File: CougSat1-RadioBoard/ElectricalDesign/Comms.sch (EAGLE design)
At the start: 409 parts, among them J1 230mm Antenna, J2 CougSat Card, J3 700mm Antenna, J4 SWD, Q1 CSD25402Q3A, Q12 DMN53D0LDW, Q2 CSD25402Q3A, Q3 DMN53D0LDW, Q9 DMN53D0LDW, U1 INA199C1, U10 HMC452QS16G, U11 AD8515, U12 AD7291, U13 AD8515, U14 LP5907MFX-3.1, U15 AD9761, U16 TXS0102DQM, U18 TXS0102DQM, U19 MMZ09332B, U2 LP5907MFX-3.1, U20 ADF4360, U21 HMC545A, U22 AD9761, U23 MAAM-011229, U24 AD8515, U25 MAAM-011229, U26 AD8345, U28 AD8348, U29 AD7291, U3 TPS61236, U30 TXS0102DQM, U31 MAAM-011229, U32 AD8515, U35 TXS0102DQM, U36 ADF4360, U37 MAAM-011229, U39 AD8515, U4 AD8346, U40 AD8515, U42 TXS0102DQM, U43 INA199C2, U44 TXS0102DQM, U45 TXS0102DQM, U46 TXS0102DQM, U47 TXS0102DQM, U48 AD7291, U49 AD8515, U5 ADF4360, U50 INA199C2, U51 LP5907MFX-3.1, U52 INA199C2, U53 INA199C1, U54 TXS0102DQM, U55 TXS0102DQM, U6 STM32L496VGT, U7 GRF2133, U8 IS25LP016D, U9 IS25LP016D, Y1 19.68MHz ±2.5ppm, Y2 8MHz ±10ppm, Y3 32.768kHz ±10ppm, Y4 19.68MHz ±2.5ppm, Y5 19.68MHz ±2.5ppm

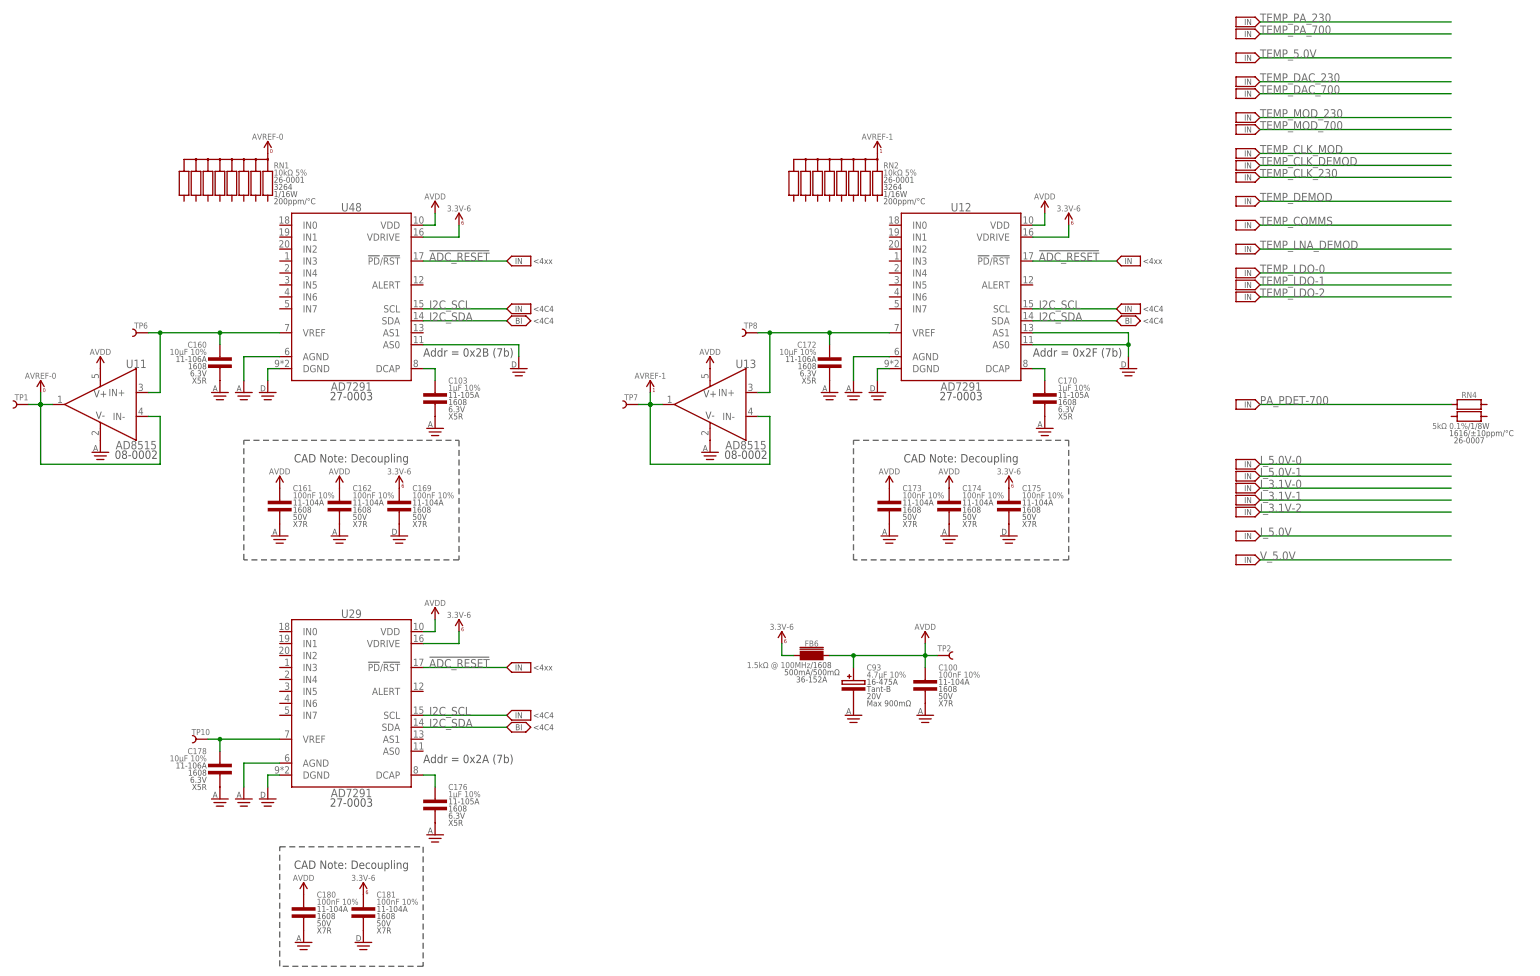
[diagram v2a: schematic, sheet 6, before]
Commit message: Laid out SPI bus, regulator, and JTAG
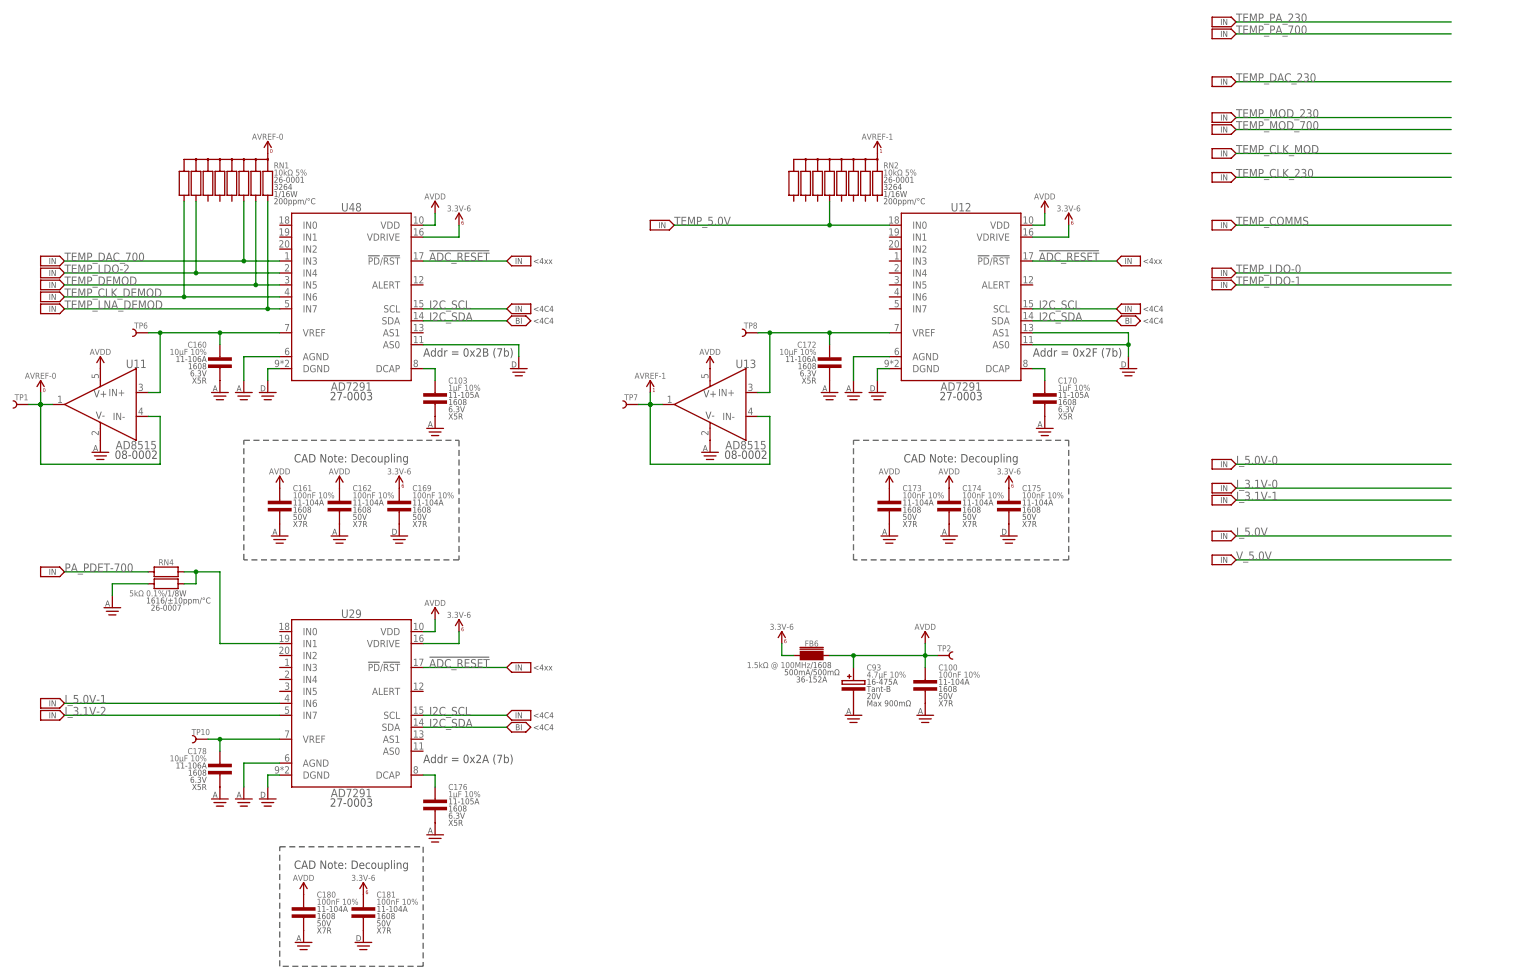
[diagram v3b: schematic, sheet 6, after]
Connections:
- net I_5.0V-1P renamed I_5.0V_1P
- new net ADC_PA_PDET-700: RN4.A2, RN4.B2, U29.IN1
- net AGND: now also RN4.A1
- net CTRL_SYNC: now also U6C.PC4; no longer U6C.PC6
- net I_3.1V-2: now also U29.IN7
- net I_5.0V-1: now also U29.IN6
- net TEMP_5.0V: now also RN2.5, U12.IN0
- net TEMP_CLK_DEMOD: now also RN1.8, U48.IN6
- net TEMP_DAC_700: now also RN1.3, U48.IN3
- net TEMP_DEMOD: now also RN1.2, U48.IN5
- net TEMP_LDO-2: now also RN1.7, U48.IN4
- net TEMP_LNA_DEMOD: now also RN1.1, U48.IN7
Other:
- moved on the sheet: RN4

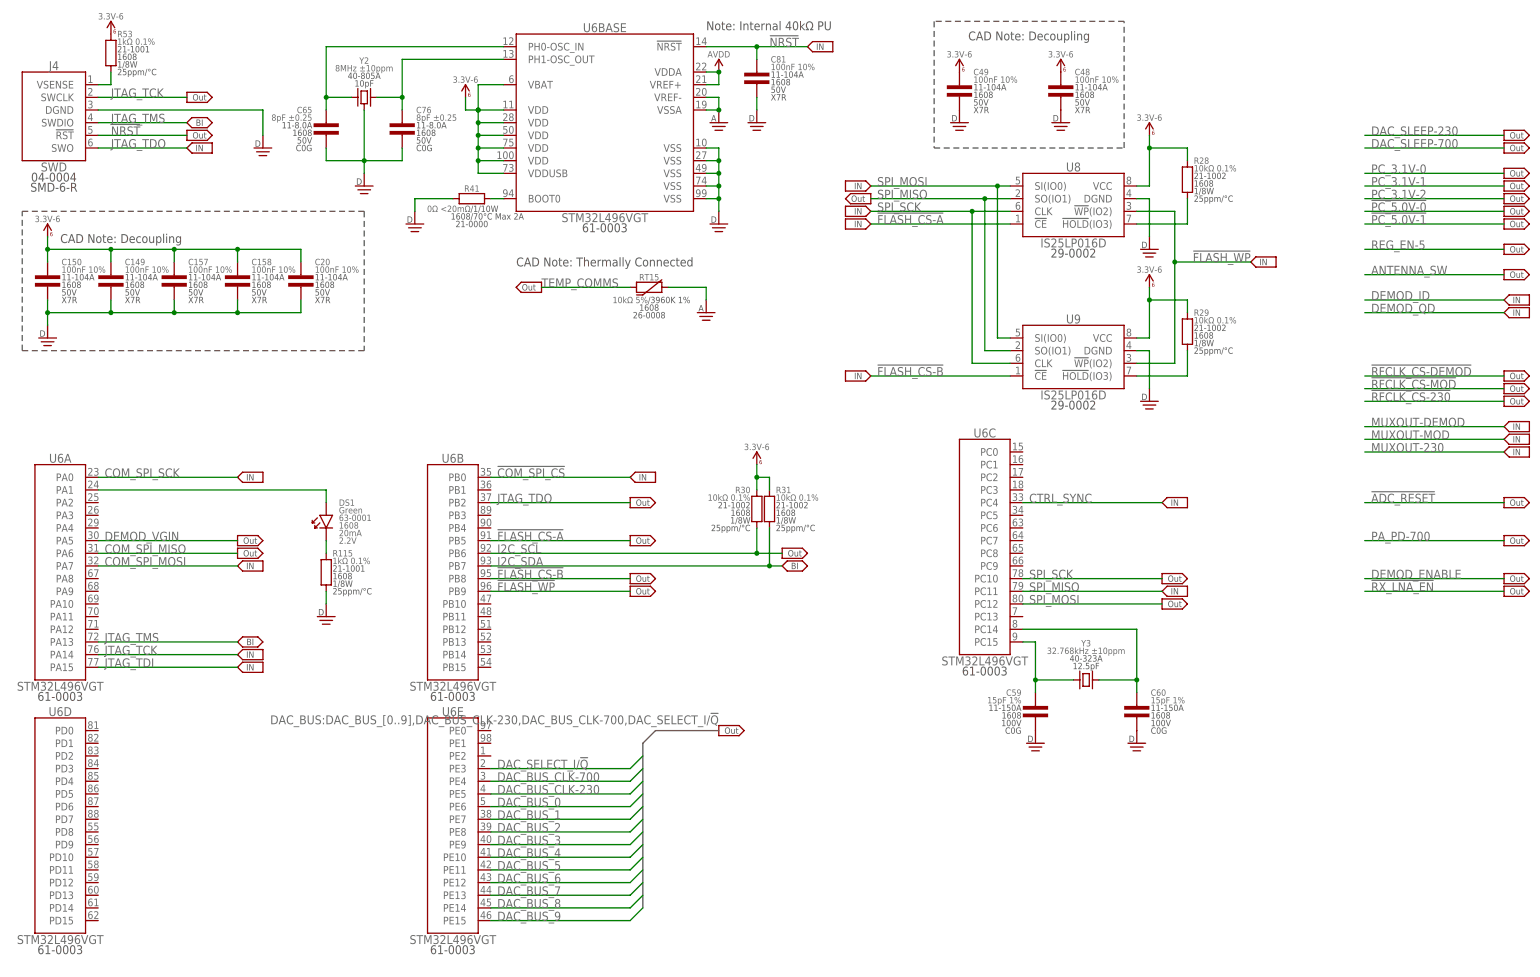
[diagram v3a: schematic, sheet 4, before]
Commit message: Laid out ADCs and 700mm thermistors and SPI
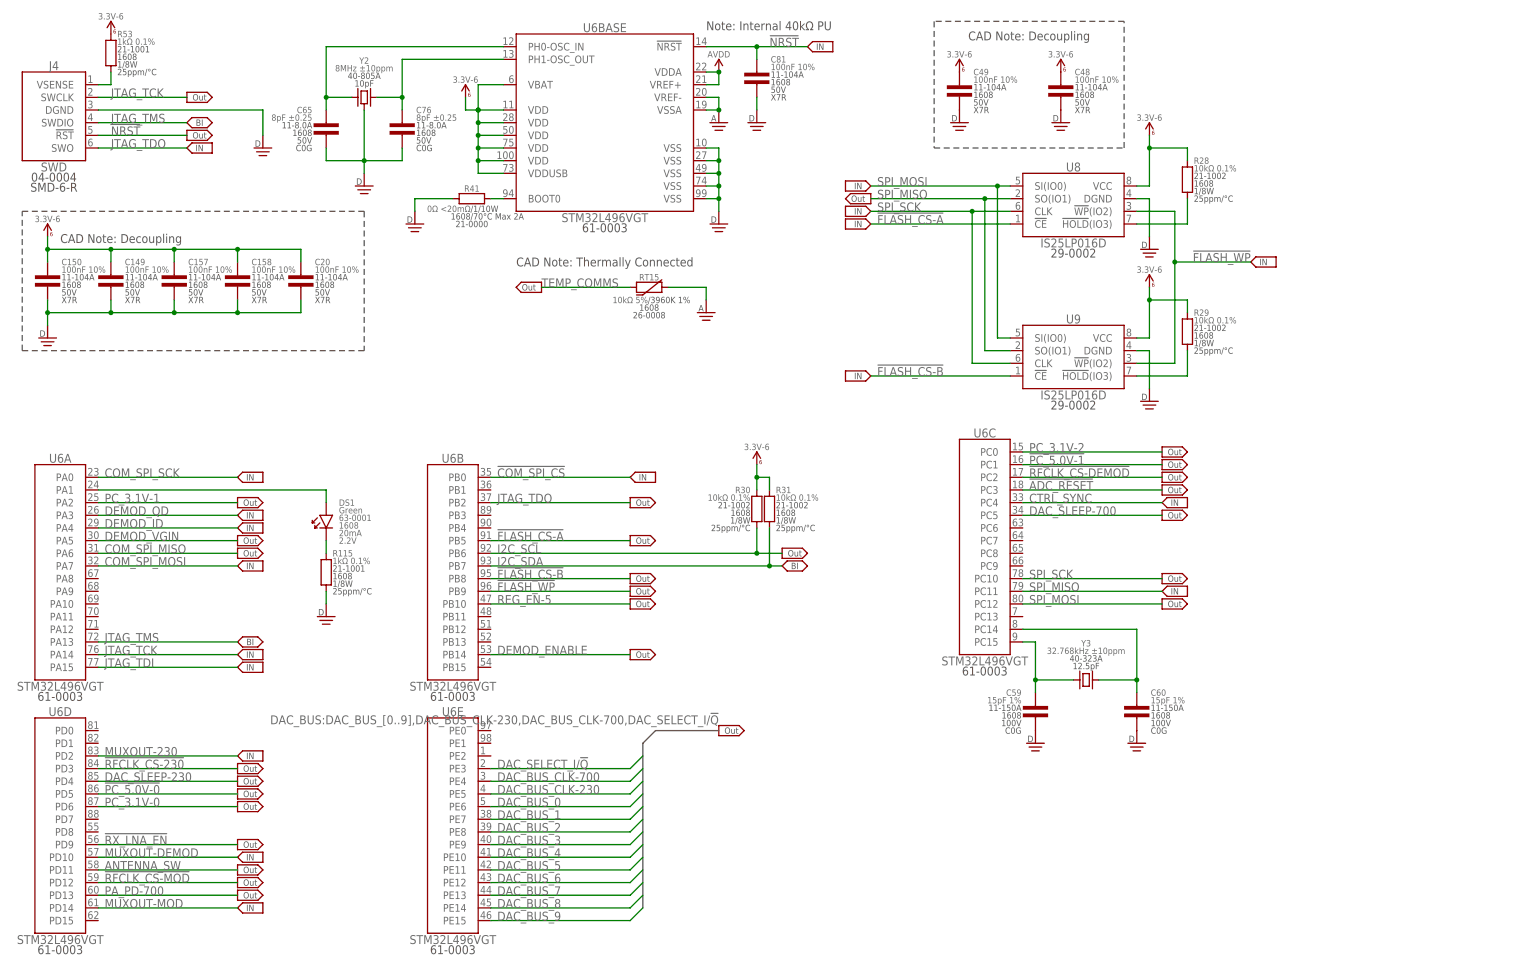
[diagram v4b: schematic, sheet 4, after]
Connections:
- net !ADC_RESET: now also U6C.PC3
- net !PC_5.0V-0: now also U6D.PD5
- net !PC_5.0V-1: now also U6C.PC1
- net !RFCLK_CS-230: now also U6D.PD3
- net !RFCLK_CS-DEMOD: now also U6C.PC2
- net !RFCLK_CS-MOD: now also U6D.PD12
- net !RX_LNA_EN: now also U6D.PD9
- net ANTENNA_SW: now also U6D.PD11
- net DAC_SLEEP-230: now also U6D.PD4
- net DAC_SLEEP-700: now also U6C.PC5
- net DEMOD_ENABLE: now also U6B.PB14
- net DEMOD_ID: now also U6A.PA4
- net DEMOD_QD: now also U6A.PA3
- net I_3.1V-0: now also U29.IN4
- net I_3.1V-1: now also U29.IN5
- net I_5.0V: now also U29.IN0
- net I_5.0V-0: now also U29.IN3
- net MUXOUT-230: now also U6D.PD2
- net MUXOUT-DEMOD: now also U6D.PD10
- net MUXOUT-MOD: now also U6D.PD14
- net PA_PD-700: now also U6D.PD13
- net PC_3.1V-0: now also U6D.PD6
- net PC_3.1V-1: now also U6A.PA2
- net PC_3.1V-2: now also U6C.PC0
- net REG_EN-5: now also U6B.PB10
- net TEMP_CLK_230: now also RN2.7, U12.IN4
- net TEMP_CLK_MOD: now also RN1.5, U48.IN0
- net TEMP_COMMS: now also RN2.4, U12.IN1
- net TEMP_DAC_230: now also RN2.6, U12.IN2
- net TEMP_LDO-0: now also RN2.3, U12.IN3
- net TEMP_LDO-1: now also RN2.1, U12.IN7
- net TEMP_MOD_230: now also RN2.8, RT2.1, U12.IN6; no longer RT9.1
- net TEMP_MOD_700: now also RN1.6, RT9.1, U48.IN2; no longer RT2.1
- net TEMP_PA_230: now also RN2.2, U12.IN5
- net TEMP_PA_700: now also RN1.4, U48.IN1
- net V_5.0V: now also U29.IN2

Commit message: Laid out remaining traces
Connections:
- net !ADC_RESET: now also U6A.PA4; no longer U6C.PC3
- net !PC_5.0V-1: now also U6C.PC2; no longer U6C.PC1
- net !RFCLK_CS-230: now also U6B.PB3; no longer U6D.PD3
- net !RFCLK_CS-DEMOD: now also U6C.PC3; no longer U6C.PC2
- net !RFCLK_CS-MOD: now also U6D.PD2; no longer U6D.PD12
- net !RX_LNA_EN: now also U6C.PC0; no longer U6D.PD9
- net ANTENNA_SW: now also U6D.PD1; no longer U6D.PD11
- net DAC_SLEEP-230: now also U6D.PD7; no longer U6D.PD4
- net DEMOD_ENABLE: now also U6A.PA2; no longer U6B.PB14
- net DEMOD_ID: now also U6A.PA1; no longer U6A.PA4
- net LED_A: now also U6D.PD8; no longer U6A.PA1
- net MUXOUT-230: now also U6B.PB4; no longer U6D.PD2
- net MUXOUT-DEMOD: now also U6D.PD0; no longer U6D.PD10
- net MUXOUT-MOD: now also U6D.PD4; no longer U6D.PD14
- net PA_PD-700: now also U6D.PD3; no longer U6D.PD13
- net PC_3.1V-1: no longer U6A.PA2
- net PC_3.1V-2: now also U6C.PC1; no longer U6C.PC0
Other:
- moved on the sheet: DS1, R115

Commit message: Adjusted silkscreen
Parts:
- removed C186, C187, C188, C189, C190: 100nF 10%, CougsInSpace-Capacitors:CAP-V-100NF-1608
- removed C192, C193: 100pF 1%, CougsInSpace-Capacitors:CAP-V-100PF-1608
- removed C194, C195: 1µF 10%, CougsInSpace-Capacitors:CAP-V-1UF-B-1608
- removed C196: 2.4pF ±0.1pF, CougsInSpace-Capacitors:CAP-V-2.4PF-1608
- removed C197, C199: 10µF 10%, CougsInSpace-Capacitors:CAP-V-10UF-3216
- removed C198, C204: 1nF 1%, CougsInSpace-Capacitors:CAP-V-1NF-B-1608
- removed C200: 0.8pF ±0.1pF, CougsInSpace-Capacitors:CAP-H-0.8PF-1608
- removed C202: 220pF 1%, CougsInSpace-Capacitors:CAP-H-220PF-1608
- removed C203: 1nF 1%, CougsInSpace-Capacitors:CAP-H-1NF-B-1608
- removed FB10: 1.5kΩ @ 100MHz, CougsInSpace-Coils:CHOKE-V-1.5K-1608
- removed H9: M2, CougsInSpace-Hardware:MOUNTING_HOLE-2.2
- removed L21: 18nH 2%, CougsInSpace-Coils:INDUCTOR-V-18NH-1608
- removed Q12, Q9: DMN53D0LDW, CougsInSpace-DiscreteSemi:MOSFET_DUAL-N-DMN53D0LDW-SOT363
- removed R101, R102, R103, R104, R107: 100kΩ 0.1%, CougsInSpace-Resistors:RES-H-100K-1608
- removed R112: 0Ω <20mΩ, CougsInSpace-Resistors:RES-V-0-1608
- removed R113, R116, R120: 10kΩ 0.1%, CougsInSpace-Resistors:RES-V-10K-1608
- removed R115: 1kΩ 0.1%, CougsInSpace-Resistors:RES-V-1K-1608
- removed R117: 20kΩ 0.5%, CougsInSpace-Resistors:RES-V-20K-1608
- removed R119: 50mΩ 1%, CougsInSpace-Resistors:RES-V-0.05R-1608
- removed RN4: 5kΩ 0.1%, CougsInSpace-Resistors:RES-H-PAIRED-5K-1616
- removed RT18, RT19, RT20: 10kΩ 5%, CougsInSpace-Resistors:THERMISTOR-H-10K-1608
- removed TP7, TP8: TEST_POINT-SMD-C-1.25, CougsInSpace-Connectors:TEST_POINT-SMD-C-1.25
- removed U50, U52: INA199C2, CougsInSpace-IC-Amplifiers:INA199C2
- removed U51: LP5907MFX-3.1, CougsInSpace-IC-Power:LDO-3.1-SOT23-5
- removed U53: INA199C1, CougsInSpace-IC-Amplifiers:INA199C1
- removed U54, U55: TXS0102DQM, CougsInSpace-IC-Comms:LEVEL_SHIFTER-2BIT-XSON-8
- added C106, C166, C22, C26, C28, C37, C38, C41, C97, C98: 100nF 10%, CougsInSpace-Capacitors:CAP-V-100NF-1608
- added C13, C36: 100pF 1%, CougsInSpace-Capacitors:CAP-V-100PF-1608
- added C142: 560pF 1%, CougsInSpace-Capacitors:CAP-V-560PF-1608
- added C23: 1nF 1%, CougsInSpace-Capacitors:CAP-H-1NF-B-1608
- added C31: 100pF 1%, CougsInSpace-Capacitors:CAP-H-100PF-1608
- added C32: 1nF 1%, CougsInSpace-Capacitors:CAP-V-1NF-B-1608
- added C92: 3.9nF 5%, CougsInSpace-Capacitors:CAP-V-3.9NF-1608
- added FB1: 1.5kΩ @ 100MHz, CougsInSpace-Coils:CHOKE-H-1.5K-1608
- added H3: Can - 230mm, CougsInSpace-Hardware:SHIELDING-2641
- added L2: 4.3nH 2%, CougsInSpace-Coils:INDUCTOR-V-4.3NH-1608
- added Q4, Q5: CSD25402Q3A, CougsInSpace-DiscreteSemi:MOSFET-P-SON-3333
- added R17: 102kΩ 0.1%, CougsInSpace-Resistors:RES-V-102K-1608
- added R18: 60.4Ω 0.1%, CougsInSpace-Resistors:RES-V-60.4R-1608
- added R23: 2kΩ 0.1%, CougsInSpace-Resistors:RES-V-2K-1608
- added R24, R25: 49.9Ω 0.1%, CougsInSpace-Resistors:RES-V-49.9-1608
- added R33: 100kΩ 0.1%, CougsInSpace-Resistors:RES-V-100K-1608
- added R46, R89: 1kΩ 0.1%, CougsInSpace-Resistors:RES-V-1K-1608
- added R88: 75Ω 0.1%, CougsInSpace-Resistors:RES-V-75R-1608
- added R9: 2kΩ 0.1%, CougsInSpace-Resistors:RES-H-2K-1608
- added R93: 50mΩ 1%, CougsInSpace-Resistors:RES-V-0.05R-1608
- added R95: 10kΩ 0.1%, CougsInSpace-Resistors:RES-V-10K-1608
- added RN3: 10kΩ 5%, CougsInSpace-Resistors:RES_BUS-10-10K-3264
- added RT12, RT3, RT8: 10kΩ 5%, CougsInSpace-Resistors:THERMISTOR-H-10K-1608
- added TP3, TP4: TEST_POINT-SMD-C-1.25, CougsInSpace-Connectors:TEST_POINT-SMD-C-1.25
- added U17: AD8515, CougsInSpace-IC-Amplifiers:OPAMP-1-AD8515
- added U27: MMZ09332B, CougsInSpace-RF:MMZ09332B
- added U33: LP5907MFX-3.1, CougsInSpace-IC-Power:LDO-3.1-SOT23-5
- added U34: MAAM-011229, CougsInSpace-RF:AMP-BIAS-MAAM-011229
- added U38: AD8346, CougsInSpace-RF:AD834X6
- added U41: HMC452QS16G, CougsInSpace-RF:AMP-BIAS-HMC452QS16G
- C1: device CougsInSpace-Capacitors:CAP-V-1UF-B-1608 -> CougsInSpace-Capacitors:CAP-V-1UF-1608
- C10, C51: value 4.7pF ±0.1 -> 100nF 10%; device CougsInSpace-Capacitors:CAP-V-4.7PF-1608 -> CougsInSpace-Capacitors:CAP-V-100NF-1608
- C101: value 1nF 1% -> 22pF 5%; device CougsInSpace-Capacitors:CAP-V-1NF-B-1608 -> CougsInSpace-Capacitors:CAP-V-22PF-1608
- C102, C62, C64, C70, C87, C99: value 1nF 1% -> 100nF 10%; device CougsInSpace-Capacitors:CAP-H-1NF-B-1608 -> CougsInSpace-Capacitors:CAP-V-100NF-1608
- C103: value 1µF 10% -> 100nF 10%; device CougsInSpace-Capacitors:CAP-V-1UF-1608 -> CougsInSpace-Capacitors:CAP-V-100NF-1608
- C104, C116, C137, C149, C168, C27, C78, C90: value 100nF 10% -> 100pF 1%; device CougsInSpace-Capacitors:CAP-V-100NF-1608 -> CougsInSpace-Capacitors:CAP-V-100PF-1608
- C105: value 1µF 10% -> 100pF 1%; device CougsInSpace-Capacitors:CAP-V-1UF-B-1608 -> CougsInSpace-Capacitors:CAP-V-100PF-1608
- C107, C50: value 100pF 1% -> 100nF 10%; device CougsInSpace-Capacitors:CAP-H-100PF-1608 -> CougsInSpace-Capacitors:CAP-V-100NF-1608
- C109: value 1µF 10% -> 2.4pF ±0.1pF; device CougsInSpace-Capacitors:CAP-V-1UF-B-1608 -> CougsInSpace-Capacitors:CAP-V-2.4PF-1608
- C11: value 10µF 10% -> 1µF 10%; device CougsInSpace-Capacitors:CAP-V-10UF-3216 -> CougsInSpace-Capacitors:CAP-V-1UF-B-1608
- C110, C185: value 100pF 1% -> 1µF 10%; device CougsInSpace-Capacitors:CAP-V-100PF-1608 -> CougsInSpace-Capacitors:CAP-V-1UF-B-1608
- C111, C29: value 10nF 10% -> 100nF 10%; device CougsInSpace-Capacitors:CAP-V-10NF-1608 -> CougsInSpace-Capacitors:CAP-V-100NF-1608
- C113: value 1nF 1% -> 2.4pF ±0.1pF; device CougsInSpace-Capacitors:CAP-V-1NF-B-1608 -> CougsInSpace-Capacitors:CAP-H-2.4PF-1608
- C115: value 1µF 10% -> 47pF 5%; device CougsInSpace-Capacitors:CAP-V-1UF-B-1608 -> CougsInSpace-Capacitors:CAP-V-47PF-1608
- C117: device CougsInSpace-Capacitors:CAP-H-1UF-B-1608 -> CougsInSpace-Capacitors:CAP-V-1UF-B-1608
- C118, C128, C20: value 100nF 10% -> 1nF 1%; device CougsInSpace-Capacitors:CAP-V-100NF-1608 -> CougsInSpace-Capacitors:CAP-V-1NF-B-1608
- C119, C33: value 56pF 2% -> 100nF 10%; device CougsInSpace-Capacitors:CAP-V-56PF-1608 -> CougsInSpace-Capacitors:CAP-V-100NF-1608
- C120: value 270pF 1% -> 1µF 10%; device CougsInSpace-Capacitors:CAP-V-270PF-1608 -> CougsInSpace-Capacitors:CAP-V-1UF-B-1608
- C121, C49: value 100nF 10% -> 1nF 1%; device CougsInSpace-Capacitors:CAP-V-100NF-1608 -> CougsInSpace-Capacitors:CAP-H-1NF-B-1608
- C122, C125, C141, C173, C174, C56, C63, C68, C72: value 100nF 10% -> 1µF 10%; device CougsInSpace-Capacitors:CAP-V-100NF-1608 -> CougsInSpace-Capacitors:CAP-V-1UF-B-1608
- C123, C138, C79: value 100nF 10% -> 10nF 10%; device CougsInSpace-Capacitors:CAP-V-100NF-1608 -> CougsInSpace-Capacitors:CAP-V-10NF-1608
- C124: value 100pF 1% -> 1nF 1%; device CougsInSpace-Capacitors:CAP-H-100PF-1608 -> CougsInSpace-Capacitors:CAP-H-1NF-B-1608
- C127, C131, C163, C165, C184, C6, C7, C8: value 1µF 10% -> 100nF 10%; device CougsInSpace-Capacitors:CAP-V-1UF-B-1608 -> CougsInSpace-Capacitors:CAP-V-100NF-1608
- C130: value 100nF 10% -> 560pF 1%; device CougsInSpace-Capacitors:CAP-V-100NF-1608 -> CougsInSpace-Capacitors:CAP-V-560PF-1608
- C132: value 100nF 10% -> 100pF 1%; device CougsInSpace-Capacitors:CAP-V-100NF-1608 -> CougsInSpace-Capacitors:CAP-H-100PF-1608
- C139, C169: value 100nF 10% -> 4.7pF ±0.1; device CougsInSpace-Capacitors:CAP-V-100NF-1608 -> CougsInSpace-Capacitors:CAP-V-4.7PF-1608
- C14: value 10µF 10% -> 100nF 10%; device CougsInSpace-Capacitors:CAP-V-10UF-3216 -> CougsInSpace-Capacitors:CAP-V-100NF-1608
- C140: value 100pF 1% -> 1µF 10%; device CougsInSpace-Capacitors:CAP-V-100PF-1608 -> CougsInSpace-Capacitors:CAP-H-1UF-B-1608
- C143, C80: value 10nF 10% -> 1nF 1%; device CougsInSpace-Capacitors:CAP-V-10NF-1608 -> CougsInSpace-Capacitors:CAP-H-1NF-B-1608
- C144: value 1nF 1% -> 100pF 1%; device CougsInSpace-Capacitors:CAP-V-1NF-B-1608 -> CougsInSpace-Capacitors:CAP-H-100PF-1608
- C145: value 1nF 1% -> 2pF ±0.1pF; device CougsInSpace-Capacitors:CAP-V-1NF-B-1608 -> CougsInSpace-Capacitors:CAP-V-2PF-1608
- C15: value 10nF 10% -> 1µF 10%; device CougsInSpace-Capacitors:CAP-V-10NF-1608 -> CougsInSpace-Capacitors:CAP-V-1UF-1608
- C151: value 10pF 5% -> 8pF ±0.25; device CougsInSpace-Capacitors:CAP-V-10PF-1608 -> CougsInSpace-Capacitors:CAP-V-8PF-1608
- C152: value 100nF 10% -> 56pF 2%; device CougsInSpace-Capacitors:CAP-V-100NF-1608 -> CougsInSpace-Capacitors:CAP-V-56PF-1608
- C153: value 100nF 10% -> 270pF 1%; device CougsInSpace-Capacitors:CAP-V-100NF-1608 -> CougsInSpace-Capacitors:CAP-V-270PF-1608
- C154: value 100nF 10% -> 10pF 5%; device CougsInSpace-Capacitors:CAP-V-100NF-1608 -> CougsInSpace-Capacitors:CAP-V-10PF-1608
- C155: value 100nF 10% -> 8pF ±0.25; device CougsInSpace-Capacitors:CAP-V-100NF-1608 -> CougsInSpace-Capacitors:CAP-V-8PF-1608
- C156: value 18pF 1% -> 100nF 10%; device CougsInSpace-Capacitors:CAP-V-18PF-1608 -> CougsInSpace-Capacitors:CAP-V-100NF-1608
- C159: value 560pF 1% -> 100nF 10%; device CougsInSpace-Capacitors:CAP-V-560PF-1608 -> CougsInSpace-Capacitors:CAP-V-100NF-1608
- C16: value 10nF 10% -> 10µF 10%; device CougsInSpace-Capacitors:CAP-V-10NF-1608 -> CougsInSpace-Capacitors:CAP-V-10UF-1608
- C160, C178: value 10µF 10% -> 100nF 10%; device CougsInSpace-Capacitors:CAP-V-10UF-1608 -> CougsInSpace-Capacitors:CAP-V-100NF-1608
- C162, C167: value 100nF 10% -> 15pF 1%; device CougsInSpace-Capacitors:CAP-V-100NF-1608 -> CougsInSpace-Capacitors:CAP-V-15PF-1608
- C164: value 100pF 1% -> 0.8pF ±0.1pF; device CougsInSpace-Capacitors:CAP-H-100PF-1608 -> CougsInSpace-Capacitors:CAP-H-0.8PF-1608
- C17, C25: value 1µF 10% -> 1nF 1%; device CougsInSpace-Capacitors:CAP-V-1UF-B-1608 -> CougsInSpace-Capacitors:CAP-V-1NF-B-1608
- C170: device CougsInSpace-Capacitors:CAP-V-1UF-1608 -> CougsInSpace-Capacitors:CAP-V-1UF-B-1608
- C171: value 560pF 1% -> 10nF 10%; device CougsInSpace-Capacitors:CAP-V-560PF-1608 -> CougsInSpace-Capacitors:CAP-V-10NF-1608
- C172: value 10µF 10% -> 1µF 10%; device CougsInSpace-Capacitors:CAP-V-10UF-1608 -> CougsInSpace-Capacitors:CAP-V-1UF-B-1608
- C176: value 1µF 10% -> 1nF 1%; device CougsInSpace-Capacitors:CAP-V-1UF-1608 -> CougsInSpace-Capacitors:CAP-H-1NF-B-1608
- C177: value 100nF 10% -> 10pF 5%; device CougsInSpace-Capacitors:CAP-V-100NF-1608 -> CougsInSpace-Capacitors:CAP-H-10PF-1608
- C181: value 100nF 10% -> 33pF 5%; device CougsInSpace-Capacitors:CAP-V-100NF-1608 -> CougsInSpace-Capacitors:CAP-H-33PF-1608
- C182: value 1µF 10% -> 33pF 5%; device CougsInSpace-Capacitors:CAP-V-1UF-B-1608 -> CougsInSpace-Capacitors:CAP-H-33PF-1608
- C19: value 1µF 10% -> 100pF 1%; device CougsInSpace-Capacitors:CAP-H-1UF-B-1608 -> CougsInSpace-Capacitors:CAP-H-100PF-1608
- C2, C4: device CougsInSpace-Capacitors:CAP-V-10UF-3216 -> CougsInSpace-Capacitors:CAP-V-10UF-1608
- C21: value 33pF 5% -> 1nF 1%; device CougsInSpace-Capacitors:CAP-H-33PF-1608 -> CougsInSpace-Capacitors:CAP-V-1NF-B-1608
- C24: value 1nF 1% -> 1µF 10%; device CougsInSpace-Capacitors:CAP-H-1NF-B-1608 -> CougsInSpace-Capacitors:CAP-H-1UF-B-1608
- C3: value 100nF 10% -> 1µF 10%; device CougsInSpace-Capacitors:CAP-V-100NF-1608 -> CougsInSpace-Capacitors:CAP-V-1UF-1608
- C30: value 33pF 5% -> 100nF 10%; device CougsInSpace-Capacitors:CAP-H-33PF-1608 -> CougsInSpace-Capacitors:CAP-V-100NF-1608
- C35: value 10nF 10% -> 1nF 1%; device CougsInSpace-Capacitors:CAP-V-10NF-1608 -> CougsInSpace-Capacitors:CAP-V-1NF-B-1608
- C39: value 270pF 1% -> 150pF 5%; device CougsInSpace-Capacitors:CAP-V-270PF-1608 -> CougsInSpace-Capacitors:CAP-V-150PF-1608
- C43: value 100nF 10% -> 33pF 5%; device CougsInSpace-Capacitors:CAP-V-100NF-1608 -> CougsInSpace-Capacitors:CAP-V-33PF-1608
- C44, C88: value 100pF 1% -> 100nF 10%; device CougsInSpace-Capacitors:CAP-V-100PF-1608 -> CougsInSpace-Capacitors:CAP-V-100NF-1608
- C46, C83: value 100pF 1% -> 1nF 1%; device CougsInSpace-Capacitors:CAP-V-100PF-1608 -> CougsInSpace-Capacitors:CAP-H-1NF-B-1608
- C47: value 10pF 5% -> 1nF 1%; device CougsInSpace-Capacitors:CAP-H-10PF-1608 -> CougsInSpace-Capacitors:CAP-H-1NF-B-1608
- C5: value 47µF -> 4.7µF 10%; device CougsInSpace-Capacitors:CAP-POL-V-47UF-4028 -> CougsInSpace-Capacitors:CAP-POL-V-4.7UF-4028
- C52: value 4.7pF ±0.1 -> 1nF 1%; device CougsInSpace-Capacitors:CAP-V-4.7PF-1608 -> CougsInSpace-Capacitors:CAP-V-1NF-B-1608
- C53: value 2pF ±0.1pF -> 1µF 10%; device CougsInSpace-Capacitors:CAP-V-2PF-1608 -> CougsInSpace-Capacitors:CAP-V-1UF-B-1608
- C57: value 1nF 1% -> 10nF 10%; device CougsInSpace-Capacitors:CAP-H-1NF-B-1608 -> CougsInSpace-Capacitors:CAP-V-10NF-1608
- C59: value 15pF 1% -> 100nF 10%; device CougsInSpace-Capacitors:CAP-V-15PF-1608 -> CougsInSpace-Capacitors:CAP-V-100NF-1608
- C60: value 15pF 1% -> 10µF 10%; device CougsInSpace-Capacitors:CAP-V-15PF-1608 -> CougsInSpace-Capacitors:CAP-V-10UF-3216
- C61: value 3.9nF 5% -> 10µF 10%; device CougsInSpace-Capacitors:CAP-V-3.9NF-1608 -> CougsInSpace-Capacitors:CAP-V-10UF-3216
- C65: value 8pF ±0.25 -> 1nF 1%; device CougsInSpace-Capacitors:CAP-V-8PF-1608 -> CougsInSpace-Capacitors:CAP-H-1NF-B-1608
- C66: value 150pF 5% -> 10nF 10%; device CougsInSpace-Capacitors:CAP-V-150PF-1608 -> CougsInSpace-Capacitors:CAP-V-10NF-1608
- C67: value 47pF 5% -> 4.7pF ±0.1; device CougsInSpace-Capacitors:CAP-V-47PF-1608 -> CougsInSpace-Capacitors:CAP-V-4.7PF-1608
- C69: value 3.9nF 5% -> 1nF 1%; device CougsInSpace-Capacitors:CAP-V-3.9NF-1608 -> CougsInSpace-Capacitors:CAP-H-1NF-B-1608
- C71: value 22pF 5% -> 100nF 10%; device CougsInSpace-Capacitors:CAP-V-22PF-1608 -> CougsInSpace-Capacitors:CAP-V-100NF-1608
- C73: value 33pF 5% -> 1µF 10%; device CougsInSpace-Capacitors:CAP-V-33PF-1608 -> CougsInSpace-Capacitors:CAP-V-1UF-B-1608
- C74: value 1nF 1% -> 10µF 10%; device CougsInSpace-Capacitors:CAP-V-1NF-B-1608 -> CougsInSpace-Capacitors:CAP-V-10UF-3216
- C75: value 1µF 10% -> 10µF 10%; device CougsInSpace-Capacitors:CAP-V-1UF-B-1608 -> CougsInSpace-Capacitors:CAP-V-10UF-3216
- C76: value 8pF ±0.25 -> 18pF 1%; device CougsInSpace-Capacitors:CAP-V-8PF-1608 -> CougsInSpace-Capacitors:CAP-V-18PF-1608
- C77: value 1nF 1% -> 3.9nF 5%; device CougsInSpace-Capacitors:CAP-H-1NF-B-1608 -> CougsInSpace-Capacitors:CAP-V-3.9NF-1608
- C82: value 2.4pF ±0.1pF -> 100nF 10%; device CougsInSpace-Capacitors:CAP-H-2.4PF-1608 -> CougsInSpace-Capacitors:CAP-V-100NF-1608
- C84: value 100nF 10% -> 47µF; device CougsInSpace-Capacitors:CAP-V-100NF-1608 -> CougsInSpace-Capacitors:CAP-POL-V-47UF-4028
- C85: value 1nF 1% -> 100nF 10%; device CougsInSpace-Capacitors:CAP-V-1NF-B-1608 -> CougsInSpace-Capacitors:CAP-V-100NF-1608
- C86: value 1nF 1% -> 10µF 10%; device CougsInSpace-Capacitors:CAP-H-1NF-B-1608 -> CougsInSpace-Capacitors:CAP-V-10UF-3216
- C89: value 100pF 1% -> 10nF 10%; device CougsInSpace-Capacitors:CAP-V-100PF-1608 -> CougsInSpace-Capacitors:CAP-V-10NF-1608
- C91: value 1nF 1% -> 220pF 1%; device CougsInSpace-Capacitors:CAP-V-1NF-B-1608 -> CougsInSpace-Capacitors:CAP-H-220PF-1608
- C93: value 4.7µF 10% -> 10µF 10%; device CougsInSpace-Capacitors:CAP-POL-V-4.7UF-4028 -> CougsInSpace-Capacitors:CAP-V-10UF-3216
- C94: value 1nF 1% -> 56pF 2%; device CougsInSpace-Capacitors:CAP-V-1NF-B-1608 -> CougsInSpace-Capacitors:CAP-V-56PF-1608
- C95: value 1nF 1% -> 270pF 1%; device CougsInSpace-Capacitors:CAP-H-1NF-B-1608 -> CougsInSpace-Capacitors:CAP-V-270PF-1608
- C96: value 100pF 1% -> 1nF 1%; device CougsInSpace-Capacitors:CAP-V-100PF-1608 -> CougsInSpace-Capacitors:CAP-V-1NF-B-1608
- FB6: device CougsInSpace-Coils:CHOKE-H-1.5K-1608 -> CougsInSpace-Coils:CHOKE-V-1.5K-1608
- H2: value M2 -> Can - Modulator; device CougsInSpace-Hardware:MOUNTING_HOLE-2.2 -> CougsInSpace-Hardware:SHIELDING-2641
- H4: value Can - 230mm -> M2; device CougsInSpace-Hardware:SHIELDING-2641 -> CougsInSpace-Hardware:MOUNTING_HOLE-2.2
- H7: value Can - Modulator -> M2; device CougsInSpace-Hardware:SHIELDING-2641 -> CougsInSpace-Hardware:MOUNTING_HOLE-2.2
- J1: value 230mm Antenna -> 700mm Antenna
- J3: value 700mm Antenna -> 230mm Antenna
- L1: value 1.0µH 20% -> 4.3nH 2%; device CougsInSpace-Coils:INDUCTOR-H-1UH-7575 -> CougsInSpace-Coils:INDUCTOR-V-4.3NH-1608
- L10, L9: value 4.3nH 2% -> 22nH 2%; device CougsInSpace-Coils:INDUCTOR-V-4.3NH-1608 -> CougsInSpace-Coils:INDUCTOR-V-22NH-1608
- L11: value 22nH 2% -> 3.9nH ±0.1nH; device CougsInSpace-Coils:INDUCTOR-V-22NH-1608 -> CougsInSpace-Coils:INDUCTOR-H-3.9NH-1608
- L12: value 22nH 2% -> 56nH 2%; device CougsInSpace-Coils:INDUCTOR-V-22NH-1608 -> CougsInSpace-Coils:INDUCTOR-H-56NH-1608
- L13: value 1.6nH 5% -> 22nH 2%; device CougsInSpace-Coils:INDUCTOR-V-1.6NH-1608 -> CougsInSpace-Coils:INDUCTOR-V-22NH-1608
- L15: value 5.6nH 2% -> 1.6nH 5%; device CougsInSpace-Coils:INDUCTOR-H-5.6NH-1608 -> CougsInSpace-Coils:INDUCTOR-V-1.6NH-1608
- L16: value 22nH 2% -> 1.6nH 5%; device CougsInSpace-Coils:INDUCTOR-V-22NH-1608 -> CougsInSpace-Coils:INDUCTOR-V-1.6NH-1608
- L18: value 1.6nH 5% -> 33nH 2%; device CougsInSpace-Coils:INDUCTOR-V-1.6NH-1608 -> CougsInSpace-Coils:INDUCTOR-V-33NH-1608
- L19: value 5.6nH 2% -> 18nH 2%; device CougsInSpace-Coils:INDUCTOR-V-5.6NH-1608 -> CougsInSpace-Coils:INDUCTOR-V-18NH-1608
- L20: value 56nH 2% -> 22nH 2%; device CougsInSpace-Coils:INDUCTOR-H-56NH-1608 -> CougsInSpace-Coils:INDUCTOR-V-22NH-1608
- L3: value 33nH 2% -> 1.0µH 20%; device CougsInSpace-Coils:INDUCTOR-V-33NH-1608 -> CougsInSpace-Coils:INDUCTOR-H-1UH-7575
- L4: value 22nH 2% -> 5.6nH 2%; device CougsInSpace-Coils:INDUCTOR-V-22NH-1608 -> CougsInSpace-Coils:INDUCTOR-H-5.6NH-1608
- L6: value 3.9nH ±0.1nH -> 12nH 2%; device CougsInSpace-Coils:INDUCTOR-H-3.9NH-1608 -> CougsInSpace-Coils:INDUCTOR-H-12NH-1608
- L7: device CougsInSpace-Coils:INDUCTOR-H-5.6NH-1608 -> CougsInSpace-Coils:INDUCTOR-V-5.6NH-1608
- L8: value 12nH 2% -> 5.6nH 2%; device CougsInSpace-Coils:INDUCTOR-H-12NH-1608 -> CougsInSpace-Coils:INDUCTOR-H-5.6NH-1608
- Q1, Q2: value CSD25402Q3A -> DMN53D0LDW; device CougsInSpace-DiscreteSemi:MOSFET-P-SON-3333 -> CougsInSpace-DiscreteSemi:MOSFET_DUAL-N-DMN53D0LDW-SOT363
- R1: value 50mΩ 1% -> 2kΩ 0.1%; device CougsInSpace-Resistors:RES-V-0.05R-1608 -> CougsInSpace-Resistors:RES-V-2K-1608
- R10: value 158kΩ 0.1% -> 2kΩ 0.1%; device CougsInSpace-Resistors:RES-V-158K-1608 -> CougsInSpace-Resistors:RES-H-2K-1608
- R11: value 49.9Ω 0.1% -> 2kΩ 0.1%; device CougsInSpace-Resistors:RES-V-49.9-1608 -> CougsInSpace-Resistors:RES-H-2K-1608
- R12, R20: value 4.7kΩ 0.1% -> 100kΩ 0.1%; device CougsInSpace-Resistors:RES-V-4.7K-1608 -> CougsInSpace-Resistors:RES-H-100K-1608
- R13: value 0Ω <20mΩ -> 100kΩ 0.1%; device CougsInSpace-Resistors:RES-V-0-1608 -> CougsInSpace-Resistors:RES-H-100K-1608
- R14: value 49.9Ω 0.1% -> 100kΩ 0.1%; device CougsInSpace-Resistors:RES-V-49.9-1608 -> CougsInSpace-Resistors:RES-H-100K-1608
- R16: value 102kΩ 0.1% -> 0Ω <20mΩ; device CougsInSpace-Resistors:RES-V-102K-1608 -> CougsInSpace-Resistors:RES-V-0-1608
- R19: value 5.6Ω 1% -> 100kΩ 0.1%; device CougsInSpace-Resistors:RES-V-5.6R-1608 -> CougsInSpace-Resistors:RES-H-100K-1608
- R2, R6: value 0Ω <20mΩ -> 2kΩ 0.1%; device CougsInSpace-Resistors:RES-V-0-1608 -> CougsInSpace-Resistors:RES-V-2K-1608
- R26: value 8.45kΩ 0.1% -> 2kΩ 0.1%; device CougsInSpace-Resistors:RES-V-8.45K-1608 -> CougsInSpace-Resistors:RES-V-2K-1608
- R27: value 10kΩ 0.1% -> 4.7kΩ 0.1%; device CougsInSpace-Resistors:RES-V-10K-1608 -> CougsInSpace-Resistors:RES-V-4.7K-1608
- R28: value 10kΩ 0.1% -> 100kΩ 0.1%; device CougsInSpace-Resistors:RES-V-10K-1608 -> CougsInSpace-Resistors:RES-V-100K-1608
- R29, R31: value 10kΩ 0.1% -> 470Ω 0.5%; device CougsInSpace-Resistors:RES-V-10K-1608 -> CougsInSpace-Resistors:RES-V-470R-1608
- R3: value 1MΩ 1% -> 0Ω <20mΩ; device CougsInSpace-Resistors:RES-V-1M-1608 -> CougsInSpace-Resistors:RES-V-0-1608
- R30, R44: value 10kΩ 0.1% -> 50mΩ 1%; device CougsInSpace-Resistors:RES-V-10K-1608 -> CougsInSpace-Resistors:RES-V-0.05R-1608
- R32: value 0Ω <20mΩ -> 330kΩ 1%; device CougsInSpace-Resistors:RES-V-0-1608 -> CougsInSpace-Resistors:RES-V-330K-1608
- R34, R36: value 1kΩ 0.1% -> 10kΩ 0.1%; device CougsInSpace-Resistors:RES-V-1K-1608 -> CougsInSpace-Resistors:RES-V-10K-1608
- R35: value 1kΩ 0.1% -> 0Ω <20mΩ; device CougsInSpace-Resistors:RES-V-1K-1608 -> CougsInSpace-Resistors:RES-V-0-1608
- R37: value 10kΩ 0.1% -> 158kΩ 0.1%; device CougsInSpace-Resistors:RES-V-10K-1608 -> CougsInSpace-Resistors:RES-V-158K-1608
- R38: value 698Ω 0.1% -> 1MΩ 1%; device CougsInSpace-Resistors:RES-V-698R-1608 -> CougsInSpace-Resistors:RES-V-1M-1608
- R39: value 50mΩ 1% -> 0Ω <20mΩ; device CougsInSpace-Resistors:RES-V-0.05R-1608 -> CougsInSpace-Resistors:RES-V-0-1608
- R4, R5: value 50mΩ 1% -> 10kΩ 0.1%; device CougsInSpace-Resistors:RES-V-0.05R-1608 -> CougsInSpace-Resistors:RES-V-10K-1608
- R40: value 0Ω <20mΩ -> 10kΩ 0.1%; device CougsInSpace-Resistors:RES-V-0-1608 -> CougsInSpace-Resistors:RES-V-10K-1608
- R41: value 0Ω <20mΩ -> 10kΩ 0.1%; device CougsInSpace-Resistors:RES-H-0-1608 -> CougsInSpace-Resistors:RES-V-10K-1608
- R42: value 698Ω 0.1% -> 20kΩ 0.5%; device CougsInSpace-Resistors:RES-V-698R-1608 -> CougsInSpace-Resistors:RES-V-20K-1608
- R43, R86: value 1.74kΩ 0.1% -> 10kΩ 0.1%; device CougsInSpace-Resistors:RES-V-1.74K-1608 -> CougsInSpace-Resistors:RES-V-10K-1608
- R47: value 10kΩ 0.1% -> 1kΩ 0.1%; device CougsInSpace-Resistors:RES-V-10K-1608 -> CougsInSpace-Resistors:RES-V-1K-1608
- R49: value 1.74kΩ 0.1% -> 49.9Ω 0.1%; device CougsInSpace-Resistors:RES-V-1.74K-1608 -> CougsInSpace-Resistors:RES-V-49.9-1608
- R50: value 1.33kΩ 0.1% -> 8.45kΩ 0.1%; device CougsInSpace-Resistors:RES-V-1.33K-1608 -> CougsInSpace-Resistors:RES-V-8.45K-1608
- R51, R55: value 1.33kΩ 0.1% -> 0Ω <20mΩ; device CougsInSpace-Resistors:RES-V-1.33K-1608 -> CougsInSpace-Resistors:RES-V-0-1608
- R52: value 1.33kΩ 0.1% -> 49.9Ω 0.1%; device CougsInSpace-Resistors:RES-V-1.33K-1608 -> CougsInSpace-Resistors:RES-V-49.9-1608
- R54: value 102kΩ 0.1% -> 698Ω 0.1%; device CougsInSpace-Resistors:RES-V-102K-1608 -> CougsInSpace-Resistors:RES-V-698R-1608
- R56: value 2kΩ 0.1% -> 1kΩ 0.1%; device CougsInSpace-Resistors:RES-H-2K-1608 -> CougsInSpace-Resistors:RES-V-1K-1608
- R57: value 0Ω <20mΩ -> 698Ω 0.1%; device CougsInSpace-Resistors:RES-V-0-1608 -> CougsInSpace-Resistors:RES-V-698R-1608
- R58: value 2kΩ 0.1% -> 0Ω <20mΩ; device CougsInSpace-Resistors:RES-H-2K-1608 -> CougsInSpace-Resistors:RES-V-0-1608
- R59: value 49.9Ω 0.1% -> 102kΩ 0.1%; device CougsInSpace-Resistors:RES-V-49.9-1608 -> CougsInSpace-Resistors:RES-V-102K-1608
- R60: value 49.9Ω 0.1% -> 470Ω 0.5%; device CougsInSpace-Resistors:RES-V-49.9-1608 -> CougsInSpace-Resistors:RES-V-470R-1608
- R61, R84: value 4.7kΩ 0.1% -> 0Ω <20mΩ; device CougsInSpace-Resistors:RES-V-4.7K-1608 -> CougsInSpace-Resistors:RES-V-0-1608
- R62: value 1kΩ 0.1% -> 2kΩ 0.1%; device CougsInSpace-Resistors:RES-V-1K-1608 -> CougsInSpace-Resistors:RES-V-2K-1608
- R63: value 2kΩ 0.1% -> 470Ω 0.5%; device CougsInSpace-Resistors:RES-V-2K-1608 -> CougsInSpace-Resistors:RES-V-470R-1608
- R64: value 470Ω 0.5% -> 1.74kΩ 0.1%; device CougsInSpace-Resistors:RES-V-470R-1608 -> CougsInSpace-Resistors:RES-V-1.74K-1608
- R65: value 2kΩ 0.1% -> 50mΩ 1%; device CougsInSpace-Resistors:RES-H-2K-1608 -> CougsInSpace-Resistors:RES-V-0.05R-1608
- R66: value 2kΩ 0.1% -> 10kΩ 0.1%; device CougsInSpace-Resistors:RES-H-2K-1608 -> CougsInSpace-Resistors:RES-V-10K-1608
- R67, R91: value 2kΩ 0.1% -> 4.7kΩ 0.1%; device CougsInSpace-Resistors:RES-V-2K-1608 -> CougsInSpace-Resistors:RES-V-4.7K-1608
- renumbered C191 to C45, C201 to C42, C205 to C40, FB9 to FB7, H8 to H1, R105 to R22, R106 to R15, R108 to R21, R118 to R92, TP10 to TP5
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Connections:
- net !230_CS: now also U39.B1, U44.LE; no longer U44.B1, U5.LE
- net !ADC_RESET: now also U3.!PD!/!RST, U4.!PD!/!RST, U40A.PA4, U7.!PD!/!RST; no longer U12.!PD!/!RST, U29.!PD!/!RST, U48.!PD!/!RST, U6A.PA4
- net !BUS_COM_SPI_CS: now also U25.A2; no longer U45.A2
- net !COM_SPI_CS: now also U25.B2, U40B.PB0; no longer U45.B2, U6B.PB0
- net !DEMOD_CS: now also U13.LE, U9.B1; no longer U20.LE, U55.B1
- net !FLASH_CS-A: now also U40B.PB5, U47.!CE; no longer U6B.PB5, U8.!CE
- net !FLASH_CS-B: now also U40B.PB8, U46.!CE; no longer U6B.PB8, U9.!CE
- net !FLASH_WP: now also U40B.PB9, U46.!WP!(IO2), U47.!WP!(IO2); no longer U6B.PB9, U8.!WP!(IO2), U9.!WP!(IO2)
- net !MOD_CS: now also U26.B1, U29.LE; no longer U18.B1, U36.LE
- net !NRST: now also C147.1, U40BASE.!NRST; no longer C81.1, U6BASE.!NRST
- net !PC_5.0V-0: now also Q5.G, U40D.PD5; no longer Q1.G, U6D.PD5
- net !PC_5.0V-1: now also Q4.G, R43.1, U40C.PC2; no longer Q2.G, R120.1, U6C.PC2
- net !RFCLK_CS-230: now also U39.A1, U40B.PB3; no longer U44.A1, U6B.PB3
- net !RFCLK_CS-DEMOD: now also U40C.PC3, U9.A1; no longer U55.A1, U6C.PC3
- net !RFCLK_CS-MOD: now also U26.A1, U40D.PD2; no longer U18.A1, U6D.PD2
- net !RX_LNA_EN: now also Q1B.G, Q2A.G, Q2B.G, U40C.PC0; no longer Q12B.G, Q3A.G, Q3B.G, U6C.PC0
- net 230_MOSI: now also U44.DATA; no longer U5.DATA
- net 230_SCK: now also U44.CLK; no longer U5.CLK
- net 3.1V_0: now also C131.1, C135.1, C137.1, C138.1, C148.1, C149.1, C156.1, C157.1, C161.1, C163.1, C170.1, C174.1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; no longer C134.1, C18.1, C188.1, C25.1, C27.1, C29.1, C34.1, C35.1, C44.1, C46.1, C6.1, C79.1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
- net 3.1V_1: now also C100.1, C108.1, C114.1, C118.1, C120.1, C122.1, C78.1, C79.1, C81.1, C82.1, C89.1, C90.1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; no longer C121.1, C123.1, C133.1, C135.1, C143.1, C148.1, C153.1, C189.1, C67.1, C7.1, C74.1, C88.1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
- net 3.1V_2: now also C13.1, C14.1, C25.1, C26.1, C27.1, C30.1, C32.1, C34.1, C36.1, C37.1, C41.1, C48.1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; no longer C110.1, C113.1, C131.1, C136.1, C137.1, C139.1, C140.1, C146.1, C147.1, C152.1, C154.1, C155.1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
- net 3.3V_0: now also C98.1, U24.VCCA, U25.VCCA, U32.VCCA; no longer C168.1, U45.VCCA, U46.VCCA, U47.VCCA
- net 3.3V_5: now also C119.1, U36.VCCA; no longer C138.1, U30.VCCA
- net 3.3V_6: now also C102.1, C107.1, C127.1, C133.1, C134.1, C159.1, C160.1, C166.1, C179.1, C183.1, C184.1, C28.1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; no longer C104.1, C141.1, C149.1, C157.1, C158.1, C167.1, C169.1, C175.1, C181.1, C186.1, C187.1, C190.1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
- net 5.0V: now also C67.1, C73.1, C75.1, C84.A, DS1.A, Q4.S, Q5.S, R38.2, R40.2, R41.2, R42.2, R43.2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; no longer C1.1, C10.1, C4.1, C5.A, DS2.A, Q1.S, Q2.S, R117.2, R120.2, R3.2, R44.2, R47.2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
- net 5.0V_0: now also C141.1, C144.1, C168.1, C172.1, C175.1, C185.1, L13.2, L18.2, R88.2, R93.1, U41.VBIAS, U49.IN-; no longer C109.1, C163.1, C164.1, C54.1, C8.1, C83.1, L3.2, L5.2, R20.2, R5.1, U1.IN-, U10.VBIAS
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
